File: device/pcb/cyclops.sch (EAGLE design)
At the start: 194 parts, among them Q1 NDS351AN, Q2 NDS351AN, Q3 NDS351AN, Q4 IRF510, U1 MCP4921, U10 LT1880, U11 ZXTD, U12 DG9421, U13 THS4281, U14 ZXTD, U15 MAX4564, U16 OPA1664, U2 LT1764A, U3 BD00FC0WEFJ, U4 LTM8020, U5 LT1931, U6 TPS72325, U7 TLV3701, U8 LT1711, U9 ADR03

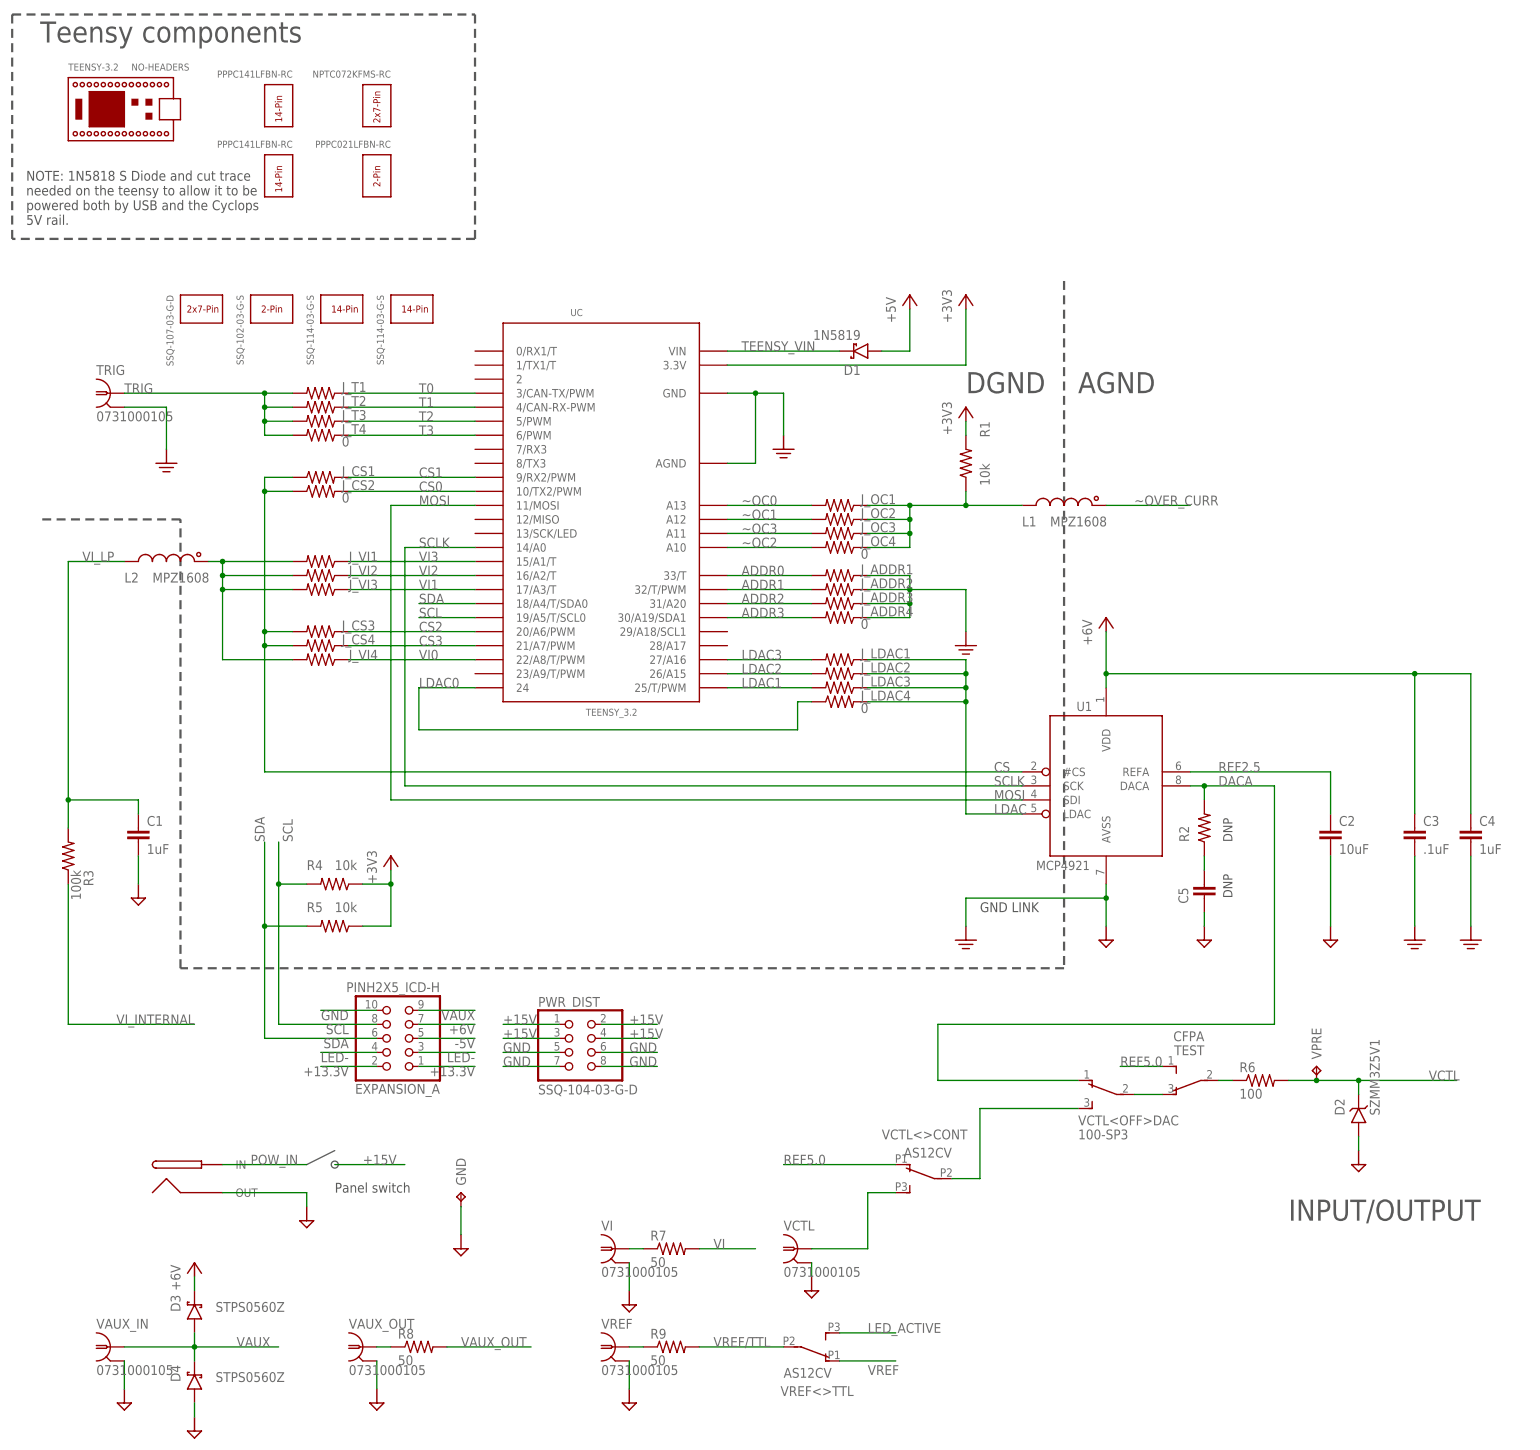
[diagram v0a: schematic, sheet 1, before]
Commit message: Schematic label clarifications.
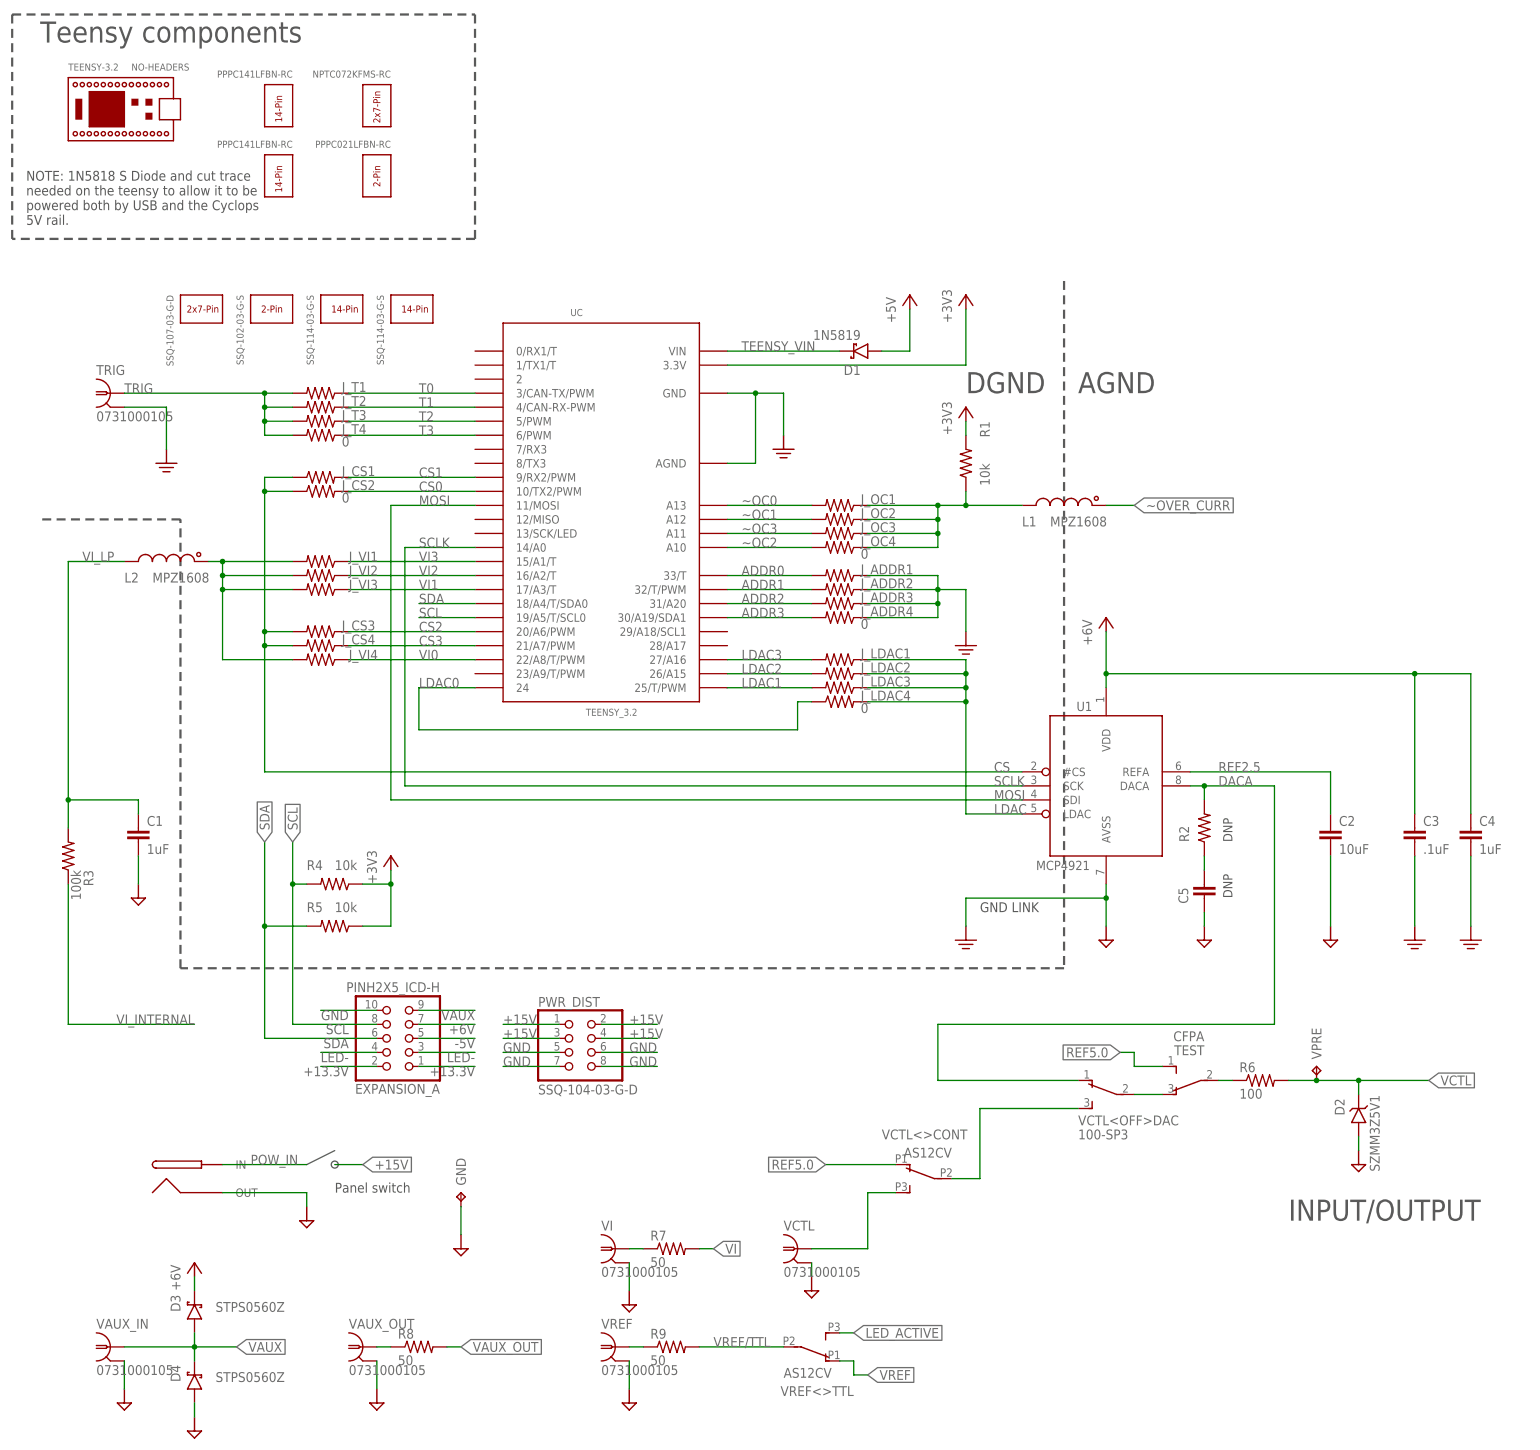
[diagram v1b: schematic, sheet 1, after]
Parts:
- renumbered REF2V1 to REF2V5, REF5V1 to REF5V0
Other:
- moved on the sheet: R23

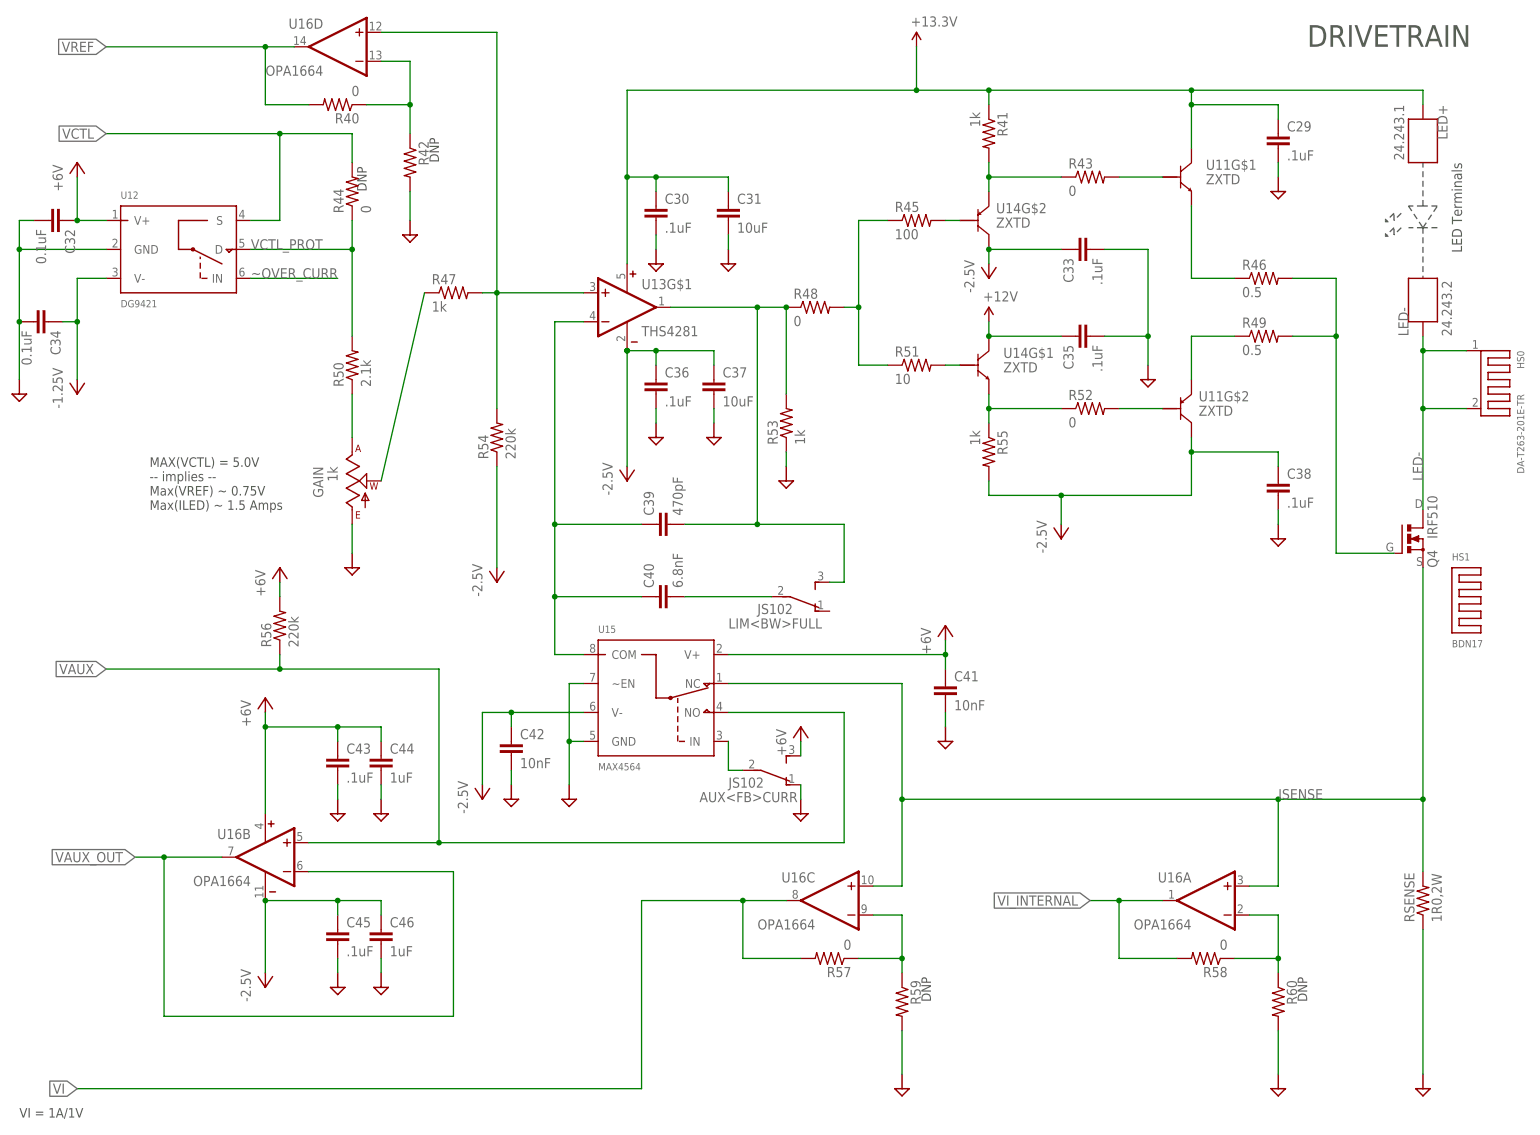
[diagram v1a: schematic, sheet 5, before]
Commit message: Level shifter and improvied thermal dissipation
- Level shifter is required since DAC's logical thresh is 0.7 VDD which
is 6V
- Improvied thermal dissiplation for FET
- Replaced finicky analog switch with a signal relay.
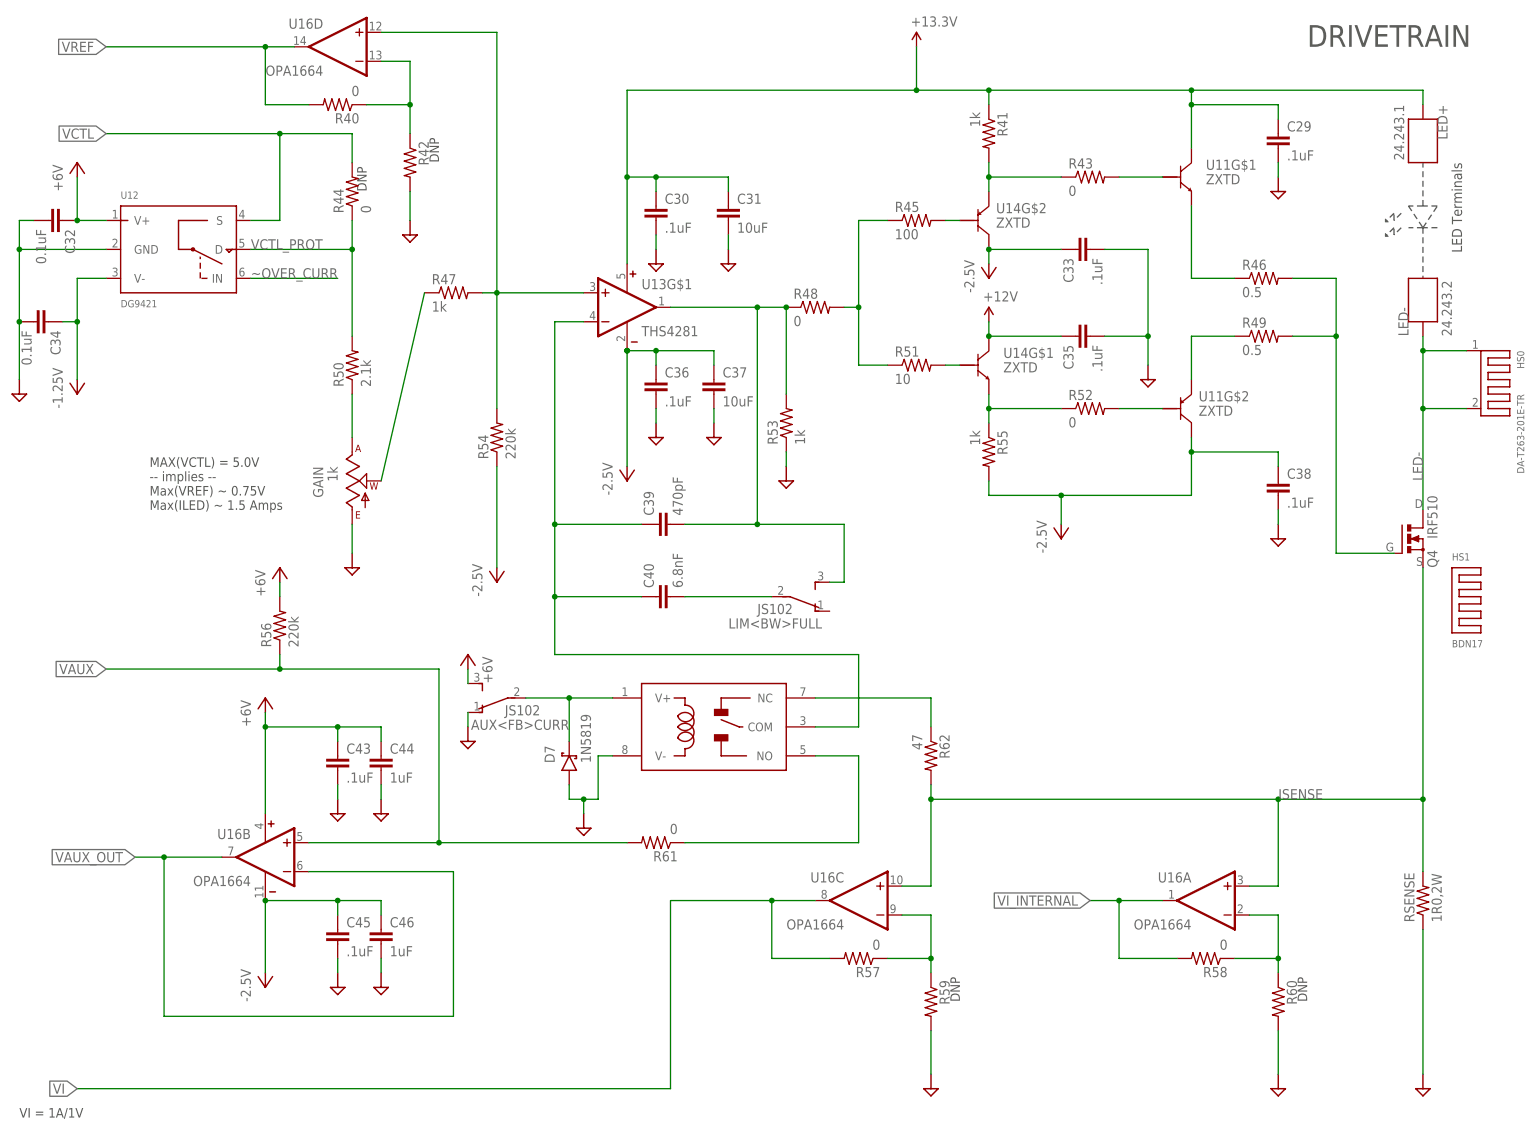
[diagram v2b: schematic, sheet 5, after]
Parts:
- removed C41, C42: 10nF, cyclops:C_0603
- removed U15: MAX4564, cyclops:MAX4564
- added C47, C48: .1uF, cyclops:C_0603
- added D7: 1N5819, jonnew:S-DIODESOD-123
- added R61: 0, cyclops:R_0603
- added R62: 47, cyclops:R_0603
- added S1: 1462042-8, jonnew:SPDT_RELAY_1462042
- added U75: TXB0104RGYR, jonnew:TXB0104_14QFN
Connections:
- removed net COM: C39.1, C40.1, U13G$1.-IN, U15.COM
- new net CS_: U1.#CS, U75.B1
- new net LDAC_: U1.LDAC, U75.B3
- new net MOSI_: U1.SDI, U75.B2
- new net N$53: C39.1, C40.1, S1.COM, U13G$1.-IN
- new net N$56: R62.1, S1.NC
- new net N$57: R61.1, S1.NO
- new net SCLK_: U1.SCK, U75.B4
- net +3V3: now also C47.1, U75.OE, U75.VCCA
- net +5V: now also C48.1, U75.VCCB
- net +6V: no longer C41.1, U15.V+
- net -2.5V: no longer C42.1, U15.V-
- net CS: now also U75.A1; no longer U1.#CS
- net GND: now also C47.2, C48.2, D7.A, S1.V-, U75.GND; no longer C41.2, C42.2, U15.GND, U15.~EN
- net IN: now also D7.C, S1.V+; no longer U15.IN
- net ISENSE: now also R62.2; no longer U15.NC
- net LDAC: now also U75.A3; no longer U1.LDAC
- net MOSI: now also U75.A2; no longer U1.SDI
- net SCLK: now also U75.A4; no longer U1.SCK
- net VAUX: now also R61.2; no longer U15.NO
- net ~OC2: now also J_OC3.2, UC.A11; no longer J_OC4.2, UC.A10
- net ~OC3: now also J_OC4.2, UC.A10; no longer J_OC3.2, UC.A11
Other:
- moved on the sheet: AUX<FB>CURR, R57, R59, U16C
